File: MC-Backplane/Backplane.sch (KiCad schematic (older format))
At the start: 6 parts

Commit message: Add files via upload
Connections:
- net ADCSlots/24vP renamed 24V
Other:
- moved on the sheet: D?, F?, J?, R?, U?
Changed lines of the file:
@@
 $Descr A4 11693 8268
 encoding utf-8
-Sheet 1 5
+Sheet 1 6
 Title ""
 Date ""
@@
 $EndDescr
 $Sheet
-S 2000 5250 950  450
-U 61E8CAB3
-F0 "GateDriveSlots" 50
-F1 "GateDriveSlots.sch" 50
-F2 "24vP" I L 2000 5350 50
-$EndSheet
-$Sheet
-S 5000 5250 950  450
+S 4950 6200 950  450
 U 61E8CB73
 F0 "DeltaSigmaSlots" 50
 F1 "DeltaSigmasSlots.sch" 50
-F2 "24vP" I L 5000 5350 50
+F2 "24V" I L 4950 6300 50
 $EndSheet
 $Sheet
-S 8550 5250 950  450
+S 4950 4700 950  450
 U 61E8CB26
 F0 "ADCSlots" 50
 F1 "ADCSlots.sch" 50
-F2 "24vP" I L 8550 5350 50
+F2 "24V" I L 4950 4800 50
 $EndSheet
 $Comp
 L Device:D_Zener D?
 U 1 1 61EB8C1B
-P 5950 2500
-F 0 "D?" V 5904 2580 50  0000 L CNN
-F 1 "Zener BZX84C9V1-7-F" V 5995 2580 50  0000 L CNN
-F 2 "" H 5950 2500 50  0001 C CNN
-F 3 "https://www.digikey.com/en/products/detail/diodes-incorporated/BZX84C9V1-7-F/717755" H 5950 2500 50  0001 C CNN
-	1    5950 2500
+P 4050 2400
+F 0 "D?" V 4004 2480 50  0000 L CNN
+F 1 "Zener BZX84C9V1-7-F" V 4095 2480 50  0000 L CNN
+F 2 "" H 4050 2400 50  0001 C CNN
+F 3 "https://www.digikey.com/en/products/detail/diodes-incorporated/BZX84C9V1-7-F/717755" H 4050 2400 50  0001 C CNN
+	1    4050 2400
 	0    1    1    0
 $EndComp
@@
 L Device:R_Small_US R?
 U 1 1 61EBB5D2
-P 5100 3150
-F 0 "R?" H 5168 3196 50  0000 L CNN
-F 1 "3k" H 5168 3105 50  0000 L CNN
-F 2 "Resistor_SMD:R_1206_3216Metric" H 5100 3150 50  0001 C CNN
-F 3 "~" H 5100 3150 50  0001 C CNN
-	1    5100 3150
+P 3200 2850
+F 0 "R?" H 3268 2896 50  0000 L CNN
+F 1 "3k" H 3268 2805 50  0000 L CNN
+F 2 "Resistor_SMD:R_1206_3216Metric" H 3200 2850 50  0001 C CNN
+F 3 "~" H 3200 2850 50  0001 C CNN
+	1    3200 2850
 	1    0    0    -1
 $EndComp
 Wire Wire Line
-	5100 2500 5100 2750
+	3200 2500 3200 2650
 Wire Wire Line
-	5950 2650 5950 2750
+	4050 2550 4050 2650
 Wire Wire Line
-	5950 2750 5100 2750
-Connection ~ 5100 2750
+	4050 2650 3200 2650
+Connection ~ 3200 2650
 Wire Wire Line
-	5100 2750 5100 3050
+	3200 2650 3200 2750
 Wire Wire Line
-	5950 2350 5950 2200
+	4050 2250 4050 2200
 Wire Wire Line
-	5950 2200 5300 2200
-Connection ~ 5950 2200
+	4050 2200 3400 2200
 $Comp
 L power:GND #PWR0101
 U 1 1 61EBD36B
-P 5100 3600
-F 0 "#PWR0101" H 5100 3350 50  0001 C CNN
-F 1 "GND" H 5105 3427 50  0000 C CNN
-F 2 "" H 5100 3600 50  0001 C CNN
-F 3 "" H 5100 3600 50  0001 C CNN
-	1    5100 3600
+P 3200 3050
+F 0 "#PWR0101" H 3200 2800 50  0001 C CNN
+F 1 "GND" H 3205 2877 50  0000 C CNN
+F 2 "" H 3200 3050 50  0001 C CNN
+F 3 "" H 3200 3050 50  0001 C CNN
+	1    3200 3050
 	1    0    0    -1
 $EndComp
@@
 RDS of PMOS needs to be really small like miliohms.\n\nDrain current needs to be larger than what the load requires.\nVDS needs to be larger than the source voltage by a significant amount. 24V so around  45V-60V.\n\nThe Zener diode needs a voltage rating of just under VDS of the mosfet. \n\nnot sure about the resistors.
 Wire Wire Line
-	5100 3250 5100 3600
-Text Notes 4500 1800 0    50   ~ 0
+	3200 2950 3200 3050
+Text Notes 2600 1800 0    50   ~ 0
 Reverse Polarity Protection Circuit
 Text Notes 8500 900  0    50   ~ 0
 Global reset to/from all cards and DSP\nFO enable b/w DSP and FO card only
-Wire Wire Line
-	1200 4250 1200 5350
-Wire Wire Line
-	1200 5350 2000 5350
-Wire Wire Line
-	4750 5350 5000 5350
-Wire Wire Line
-	4750 4950 7250 4950
-Wire Wire Line
-	8150 4950 8150 5350
-Wire Wire Line
-	8150 5350 8550 5350
-Wire Wire Line
-	4750 4950 4750 5350
 $Comp
 L MC-Backplane:64600001223 U?
 U 1 1 61F13696
-P 3650 2400
-F 0 "U?" H 3650 2427 50  0000 C CNN
-F 1 "64600001223" H 3650 2336 50  0000 C CNN
-F 2 "" H 3650 2400 50  0001 C CNN
-F 3 "https://www.littelfuse.com/~/media/electronics/datasheets/fuse_blocks/littelfuse_fuse_block_646_datasheet.pdf.pdf" H 3650 2400 50  0001 C CNN
-	1    3650 2400
+P 2300 2400
+F 0 "U?" H 2300 2427 50  0000 C CNN
+F 1 "64600001223" H 2300 2336 50  0000 C CNN
+F 2 "" H 2300 2400 50  0001 C CNN
+F 3 "https://www.littelfuse.com/~/media/electronics/datasheets/fuse_blocks/littelfuse_fuse_block_646_datasheet.pdf.pdf" H 2300 2400 50  0001 C CNN
+	1    2300 2400
 	1    0    0    -1
 $EndComp
 Wire Wire Line
-	4050 2200 4900 2200
-Wire Wire Line
-	5950 2200 7250 2200
-Wire Wire Line
-	1200 4250 7250 4250
-Wire Wire Line
-	7250 4250 7250 2200
-Connection ~ 7250 2200
-Wire Wire Line
-	7250 2200 10000 2200
-Wire Wire Line
-	7250 4250 7250 4950
-Connection ~ 7250 4250
-Connection ~ 7250 4950
-Wire Wire Line
-	7250 4950 8150 4950
+	2700 2200 3000 2200
 $Comp
 L Connector:Barrel_Jack J?
 U 1 1 61F21CB0
-P 1850 2300
-F 0 "J?" H 1907 2625 50  0000 C CNN
-F 1 "Barrel_Jack" H 1907 2534 50  0000 C CNN
-F 2 "" H 1900 2260 50  0001 C CNN
-F 3 "~" H 1900 2260 50  0001 C CNN
-	1    1850 2300
+P 1300 2300
+F 0 "J?" H 1357 2625 50  0000 C CNN
+F 1 "Barrel_Jack" H 1357 2534 50  0000 C CNN
+F 2 "" H 1350 2260 50  0001 C CNN
+F 3 "~" H 1350 2260 50  0001 C CNN
+	1    1300 2300
 	1    0    0    -1
 $EndComp
 Wire Wire Line
-	2150 2200 3250 2200
+	1600 2200 1900 2200
 $Comp
 L Device:Fuse F?
 U 1 1 61F2B17A
-P 3650 1700
-F 0 "F?" V 3453 1700 50  0000 C CNN
-F 1 "Fuse" V 3544 1700 50  0000 C CNN
-F 2 "" V 3580 1700 50  0001 C CNN
-F 3 "~" H 3650 1700 50  0001 C CNN
-	1    3650 1700
+P 2300 1700
+F 0 "F?" V 2103 1700 50  0000 C CNN
+F 1 "Fuse" V 2194 1700 50  0000 C CNN
+F 2 "" V 2230 1700 50  0001 C CNN
+F 3 "~" H 2300 1700 50  0001 C CNN
+	1    2300 1700
 	0    1    1    0
 $EndComp
 Wire Wire Line
-	3500 1700 3500 1950
+	2150 1700 2150 1950
 Wire Wire Line
-	3800 1950 3800 1700
-Text Notes 1400 2650 0    50   ~ 0
+	2450 1950 2450 1700
+Text Notes 850  2650 0    50   ~ 0
 maybe:  5.5mm barrel jack? \nwith 2.1mm center pole
 $Comp
 L MC-Backplane:SISS05DN-T1-GE3 U?
 U 1 1 61F2E911
-P 5600 2200
-F 0 "U?" V 5842 2700 50  0000 C CNN
-F 1 "SISS05DN-T1-GE3" V 5751 2700 50  0000 C CNN
-F 2 "" H 5600 2200 50  0001 C CNN
-F 3 "" H 5600 2200 50  0001 C CNN
-	1    5600 2200
+P 3700 2200
+F 0 "U?" V 3942 2700 50  0000 C CNN
+F 1 "SISS05DN-T1-GE3" V 3851 2700 50  0000 C CNN
+F 2 "" H 3700 2200 50  0001 C CNN
+F 3 "" H 3700 2200 50  0001 C CNN
+	1    3700 2200
 	0    -1   -1   0
 $EndComp
 $Sheet
-S 10000 2100 950  1900
+S 9400 1700 1000 3950
 U 61E8CBE3
 F0 "DSPSlot" 50
 F1 "DSPSlot.sch" 50
-F2 "24vP" I L 10000 2200 50
+F2 "24V" I L 9400 1800 50
 $EndSheet
+$Sheet
+S 1750 3550 1150 1450
+U 61E8CAB3
+F0 "GateDriveSlots" 50
+F1 "GateDriveSlots.sch" 50
+F2 "24V" I L 1750 3600 50
+F3 "GND" I R 2900 4950 50
+F4 "EPWM1_1A" I L 1750 3750 50
+F5 "EPWM1_1B" I L 1750 3850 50
+F6 "RESET1_1" I L 1750 3950 50
+F7 "STATUS1_1" O R 2900 3600 50
+F8 "EPWM1_2A" I L 1750 4050 50
+F9 "EPWM1_2B" I L 1750 4150 50
+F10 "RESET1_2" I L 1750 4250 50
+F11 "STATUS1_2" O R 2900 3700 50
+F12 "EPWM3_1A" I L 1750 4400 50
+F13 "EPWM3_1B" I L 1750 4500 50
+F14 "STATUS3_1" O R 2900 4000 50
+F15 "EPWM3_2A" I L 1750 4650 50
+F16 "EPWM3_2B" I L 1750 4750 50
+F17 "RESET3_2" I L 1750 4850 50
+F18 "EPWM2_1A" I R 2900 4300 50
+F19 "EPWM2_1B" I R 2900 4400 50
+F20 "RESET2_1" I R 2900 4500 50
+F21 "STATUS2_1" O R 2900 3800 50
+F22 "EPWM2_2A" I R 2900 4600 50
+F23 "EPWM2_2B" I R 2900 4700 50
+F24 "RESET2_2" I R 2900 4800 50
+F25 "STATUS2_2" O R 2900 3900 50
+F26 "STATUS3_2" O R 2900 4100 50
+$EndSheet
+$Sheet
+S 1750 5600 1150 1500
+U 61F59C33
+F0 "GateDriveSlots4-6" 50
+F1 "GateDriveSlots4-6.sch" 50
+F2 "24V" I L 1750 5700 50
+$EndSheet
+Wire Wire Line
+	4050 2200 4700 2200
+Connection ~ 4050 2200
+Text GLabel 4700 2200 2    50   Output ~ 0
+24V
+Text GLabel 1750 3600 0    50   Input ~ 0
+24V
+Text GLabel 1750 5700 0    50   Input ~ 0
+24V
+Text GLabel 4950 6300 0    50   Input ~ 0
+24V
+Text GLabel 4950 4800 0    50   Input ~ 0
+24V
+Text GLabel 9400 1800 0    50   Input ~ 0
+24V
 $EndSCHEMATC

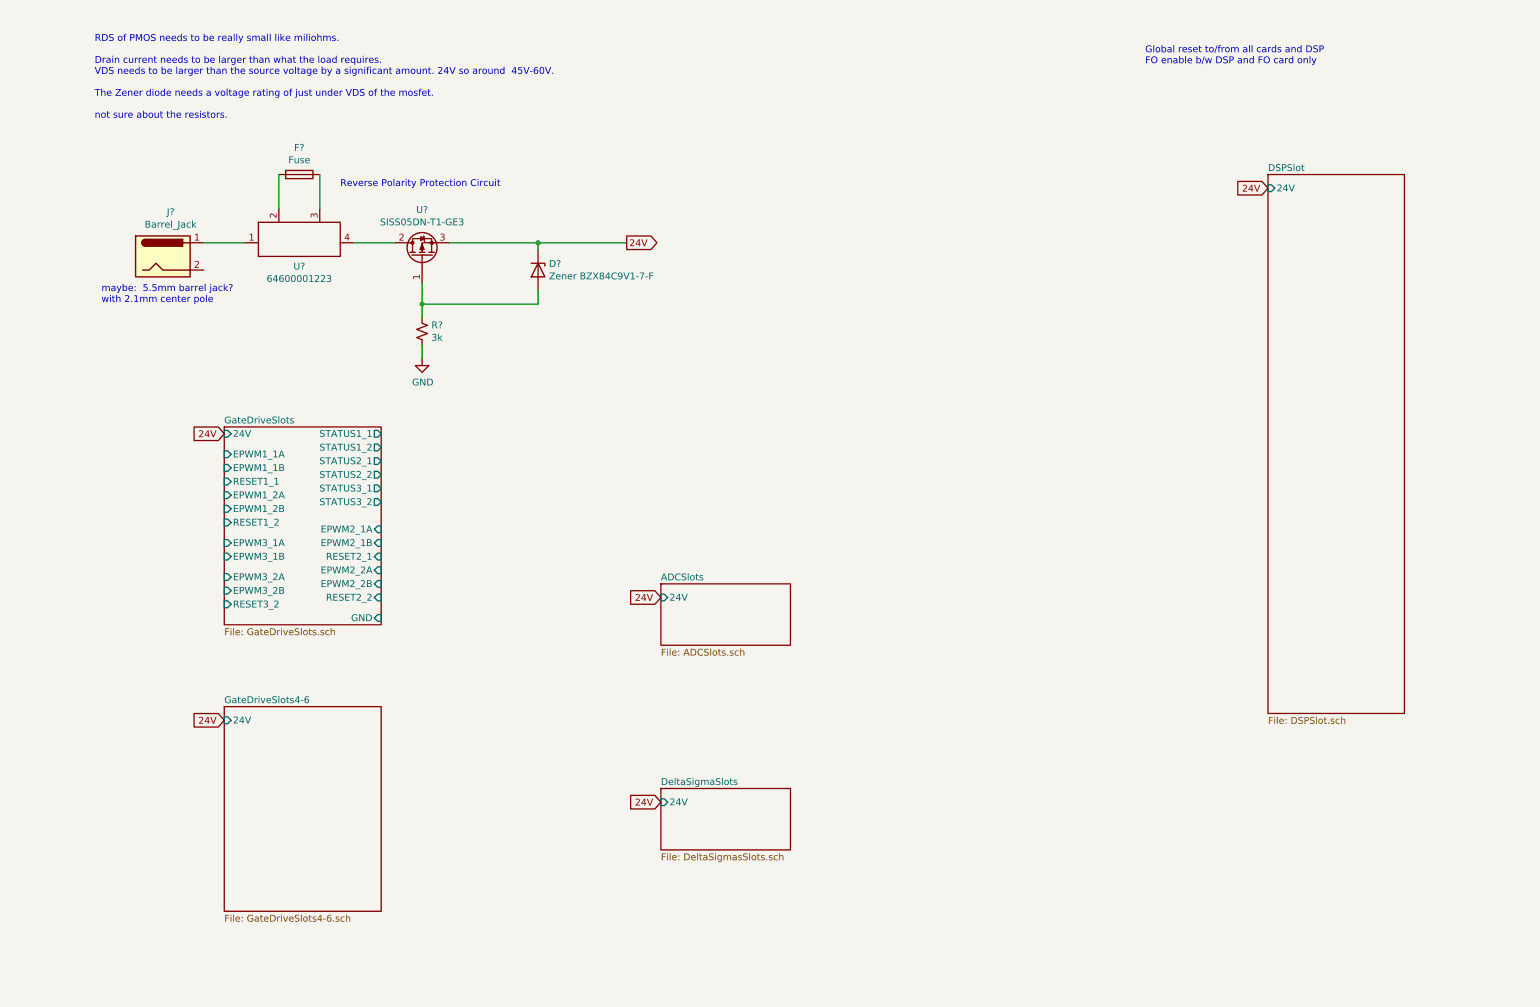
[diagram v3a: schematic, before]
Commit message: added signals for FO slots
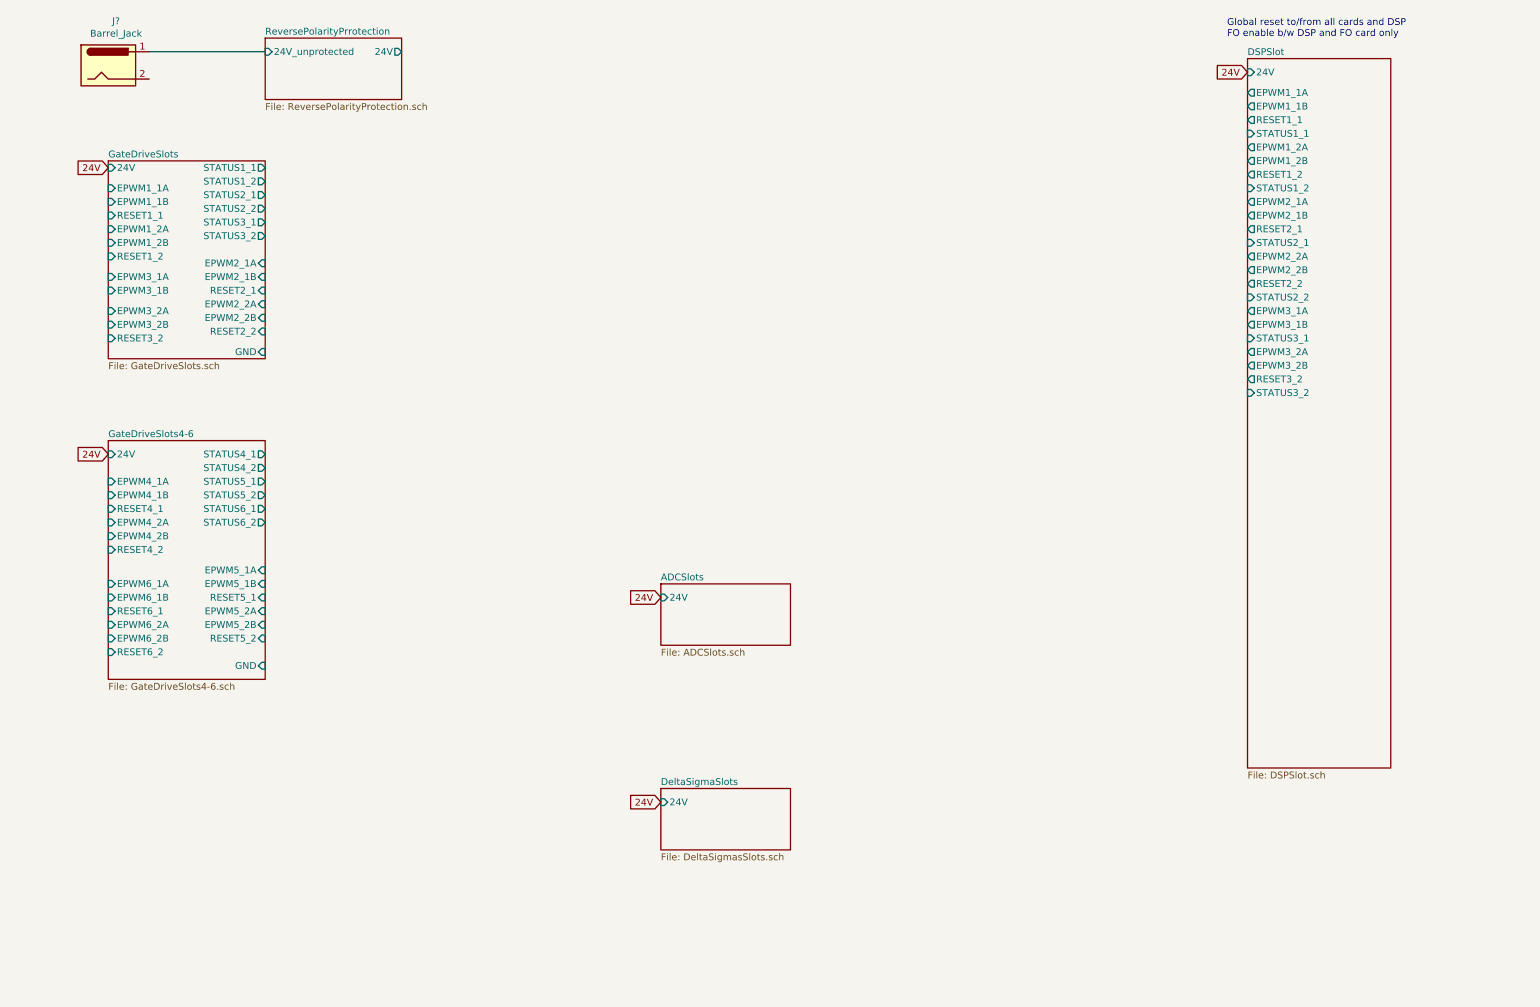
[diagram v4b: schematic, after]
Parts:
- removed D?: Zener BZX84C9V1-7-F, symbol Device:D_Zener
- removed F?: Fuse, symbol Device:Fuse
- removed R?: 3k, Resistor_SMD:R_1206_3216Metric, symbol Device:R_Small_US
- removed U?: 64600001223, symbol MC-Backplane:64600001223
- removed U?: SISS05DN-T1-GE3, symbol MC-Backplane:SISS05DN-T1-GE3
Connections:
- net ReversePolarityPrrotection/24V_unprotected: now reaches J?.1
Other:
- note removed: "RDS of PMOS needs to be really small like miliohms.\n\nDrain current needs to be larger than what the load requires.\nVDS needs to be larger than the source voltage by a significant amount. 24V so around 45V-60V.\n\nThe Zener diode needs a voltage rating of just under VDS of the mosfet. \n\nnot sure about the resistors."
- note removed: "Reverse Polarity Protection Circuit"
- note removed: "maybe: 5.5mm barrel jack? \nwith 2.1mm center pole"
- moved on the sheet: J?
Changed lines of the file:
@@
 $Descr A4 11693 8268
 encoding utf-8
-Sheet 1 6
+Sheet 1 7
 Title ""
 Date ""
@@
 F2 "24V" I L 4950 4800 50
 $EndSheet
-$Comp
-L Device:D_Zener D?
-U 1 1 61EB8C1B
-P 4050 2400
-F 0 "D?" V 4004 2480 50  0000 L CNN
-F 1 "Zener BZX84C9V1-7-F" V 4095 2480 50  0000 L CNN
-F 2 "" H 4050 2400 50  0001 C CNN
-F 3 "https://www.digikey.com/en/products/detail/diodes-incorporated/BZX84C9V1-7-F/717755" H 4050 2400 50  0001 C CNN
-	1    4050 2400
-	0    1    1    0
-$EndComp
-$Comp
-L Device:R_Small_US R?
-U 1 1 61EBB5D2
-P 3200 2850
-F 0 "R?" H 3268 2896 50  0000 L CNN
-F 1 "3k" H 3268 2805 50  0000 L CNN
-F 2 "Resistor_SMD:R_1206_3216Metric" H 3200 2850 50  0001 C CNN
-F 3 "~" H 3200 2850 50  0001 C CNN
-	1    3200 2850
-	1    0    0    -1
-$EndComp
-Wire Wire Line
-	3200 2500 3200 2650
-Wire Wire Line
-	4050 2550 4050 2650
-Wire Wire Line
-	4050 2650 3200 2650
-Connection ~ 3200 2650
-Wire Wire Line
-	3200 2650 3200 2750
-Wire Wire Line
-	4050 2250 4050 2200
-Wire Wire Line
-	4050 2200 3400 2200
-$Comp
-L power:GND #PWR0101
-U 1 1 61EBD36B
-P 3200 3050
-F 0 "#PWR0101" H 3200 2800 50  0001 C CNN
-F 1 "GND" H 3205 2877 50  0000 C CNN
-F 2 "" H 3200 3050 50  0001 C CNN
-F 3 "" H 3200 3050 50  0001 C CNN
-	1    3200 3050
-	1    0    0    -1
-$EndComp
-Text Notes 800  1300 0    50   ~ 0
-RDS of PMOS needs to be really small like miliohms.\n\nDrain current needs to be larger than what the load requires.\nVDS needs to be larger than the source voltage by a significant amount. 24V so around  45V-60V.\n\nThe Zener diode needs a voltage rating of just under VDS of the mosfet. \n\nnot sure about the resistors.
-Wire Wire Line
-	3200 2950 3200 3050
-Text Notes 2600 1800 0    50   ~ 0
-Reverse Polarity Protection Circuit
-Text Notes 8500 900  0    50   ~ 0
+Text Notes 9100 700  0    50   ~ 0
 Global reset to/from all cards and DSP\nFO enable b/w DSP and FO card only
-$Comp
-L MC-Backplane:64600001223 U?
-U 1 1 61F13696
-P 2300 2400
-F 0 "U?" H 2300 2427 50  0000 C CNN
-F 1 "64600001223" H 2300 2336 50  0000 C CNN
-F 2 "" H 2300 2400 50  0001 C CNN
-F 3 "https://www.littelfuse.com/~/media/electronics/datasheets/fuse_blocks/littelfuse_fuse_block_646_datasheet.pdf.pdf" H 2300 2400 50  0001 C CNN
-	1    2300 2400
-	1    0    0    -1
-$EndComp
-Wire Wire Line
-	2700 2200 3000 2200
 $Comp
 L Connector:Barrel_Jack J?
 U 1 1 61F21CB0
-P 1300 2300
-F 0 "J?" H 1357 2625 50  0000 C CNN
-F 1 "Barrel_Jack" H 1357 2534 50  0000 C CNN
-F 2 "" H 1350 2260 50  0001 C CNN
-F 3 "~" H 1350 2260 50  0001 C CNN
-	1    1300 2300
+P 900 900
+F 0 "J?" H 957 1225 50  0000 C CNN
+F 1 "Barrel_Jack" H 957 1134 50  0000 C CNN
+F 2 "" H 950 860 50  0001 C CNN
+F 3 "~" H 950 860 50  0001 C CNN
+	1    900  900
 	1    0    0    -1
 $EndComp
-Wire Wire Line
-	1600 2200 1900 2200
-$Comp
-L Device:Fuse F?
-U 1 1 61F2B17A
-P 2300 1700
-F 0 "F?" V 2103 1700 50  0000 C CNN
-F 1 "Fuse" V 2194 1700 50  0000 C CNN
-F 2 "" V 2230 1700 50  0001 C CNN
-F 3 "~" H 2300 1700 50  0001 C CNN
-	1    2300 1700
-	0    1    1    0
-$EndComp
-Wire Wire Line
-	2150 1700 2150 1950
-Wire Wire Line
-	2450 1950 2450 1700
-Text Notes 850  2650 0    50   ~ 0
-maybe:  5.5mm barrel jack? \nwith 2.1mm center pole
-$Comp
-L MC-Backplane:SISS05DN-T1-GE3 U?
-U 1 1 61F2E911
-P 3700 2200
-F 0 "U?" V 3942 2700 50  0000 C CNN
-F 1 "SISS05DN-T1-GE3" V 3851 2700 50  0000 C CNN
-F 2 "" H 3700 2200 50  0001 C CNN
-F 3 "" H 3700 2200 50  0001 C CNN
-	1    3700 2200
-	0    -1   -1   0
-$EndComp
 $Sheet
-S 9400 1700 1000 3950
+S 9250 850  1050 5200
 U 61E8CBE3
 F0 "DSPSlot" 50
 F1 "DSPSlot.sch" 50
-F2 "24V" I L 9400 1800 50
+F2 "24V" I L 9250 950 50
+F3 "EPWM1_1A" O L 9250 1100 50
+F4 "EPWM1_1B" O L 9250 1200 50
+F5 "RESET1_1" O L 9250 1300 50
+F6 "STATUS1_1" I L 9250 1400 50
+F7 "EPWM1_2A" O L 9250 1500 50
+F8 "EPWM1_2B" O L 9250 1600 50
+F9 "RESET1_2" O L 9250 1700 50
+F10 "STATUS1_2" I L 9250 1800 50
+F11 "EPWM2_1A" O L 9250 1900 50
+F12 "EPWM2_1B" O L 9250 2000 50
+F13 "RESET2_1" O L 9250 2100 50
+F14 "STATUS2_1" I L 9250 2200 50
+F15 "EPWM2_2A" O L 9250 2300 50
+F16 "EPWM2_2B" O L 9250 2400 50
+F17 "RESET2_2" O L 9250 2500 50
+F18 "STATUS2_2" I L 9250 2600 50
+F19 "EPWM3_1A" O L 9250 2700 50
+F20 "EPWM3_1B" O L 9250 2800 50
+F21 "STATUS3_1" I L 9250 2900 50
+F22 "EPWM3_2A" O L 9250 3000 50
+F23 "EPWM3_2B" O L 9250 3100 50
+F24 "RESET3_2" O L 9250 3200 50
+F25 "STATUS3_2" I L 9250 3300 50
 $EndSheet
 $Sheet
-S 1750 3550 1150 1450
+S 900  1600 1150 1450
 U 61E8CAB3
 F0 "GateDriveSlots" 50
 F1 "GateDriveSlots.sch" 50
-F2 "24V" I L 1750 3600 50
-F3 "GND" I R 2900 4950 50
-F4 "EPWM1_1A" I L 1750 3750 50
-F5 "EPWM1_1B" I L 1750 3850 50
-F6 "RESET1_1" I L 1750 3950 50
-F7 "STATUS1_1" O R 2900 3600 50
-F8 "EPWM1_2A" I L 1750 4050 50
-F9 "EPWM1_2B" I L 1750 4150 50
-F10 "RESET1_2" I L 1750 4250 50
-F11 "STATUS1_2" O R 2900 3700 50
-F12 "EPWM3_1A" I L 1750 4400 50
-F13 "EPWM3_1B" I L 1750 4500 50
-F14 "STATUS3_1" O R 2900 4000 50
-F15 "EPWM3_2A" I L 1750 4650 50
-F16 "EPWM3_2B" I L 1750 4750 50
-F17 "RESET3_2" I L 1750 4850 50
-F18 "EPWM2_1A" I R 2900 4300 50
-F19 "EPWM2_1B" I R 2900 4400 50
-F20 "RESET2_1" I R 2900 4500 50
-F21 "STATUS2_1" O R 2900 3800 50
-F22 "EPWM2_2A" I R 2900 4600 50
-F23 "EPWM2_2B" I R 2900 4700 50
-F24 "RESET2_2" I R 2900 4800 50
-F25 "STATUS2_2" O R 2900 3900 50
-F26 "STATUS3_2" O R 2900 4100 50
+F2 "24V" I L 900 1650 50
+F3 "GND" I R 2050 3000 50
+F4 "EPWM1_1A" I L 900 1800 50
+F5 "EPWM1_1B" I L 900 1900 50
+F6 "RESET1_1" I L 900 2000 50
+F7 "STATUS1_1" O R 2050 1650 50
+F8 "EPWM1_2A" I L 900 2100 50
+F9 "EPWM1_2B" I L 900 2200 50
+F10 "RESET1_2" I L 900 2300 50
+F11 "STATUS1_2" O R 2050 1750 50
+F12 "EPWM3_1A" I L 900 2450 50
+F13 "EPWM3_1B" I L 900 2550 50
+F14 "STATUS3_1" O R 2050 2050 50
+F15 "EPWM3_2A" I L 900 2700 50
+F16 "EPWM3_2B" I L 900 2800 50
+F17 "RESET3_2" I L 900 2900 50
+F18 "EPWM2_1A" I R 2050 2350 50
+F19 "EPWM2_1B" I R 2050 2450 50
+F20 "RESET2_1" I R 2050 2550 50
+F21 "STATUS2_1" O R 2050 1850 50
+F22 "EPWM2_2A" I R 2050 2650 50
+F23 "EPWM2_2B" I R 2050 2750 50
+F24 "RESET2_2" I R 2050 2850 50
+F25 "STATUS2_2" O R 2050 1950 50
+F26 "STATUS3_2" O R 2050 2150 50
 $EndSheet
-$Sheet
-S 1750 5600 1150 1500
-U 61F59C33
-F0 "GateDriveSlots4-6" 50
-F1 "GateDriveSlots4-6.sch" 50
-F2 "24V" I L 1750 5700 50
-$EndSheet
-Wire Wire Line
-	4050 2200 4700 2200
-Connection ~ 4050 2200
-Text GLabel 4700 2200 2    50   Output ~ 0
-24V
-Text GLabel 1750 3600 0    50   Input ~ 0
-24V
-Text GLabel 1750 5700 0    50   Input ~ 0
+Text GLabel 900  1650 0    50   Input ~ 0
 24V
 Text GLabel 4950 6300 0    50   Input ~ 0
@@
 Text GLabel 4950 4800 0    50   Input ~ 0
 24V
-Text GLabel 9400 1800 0    50   Input ~ 0
+Text GLabel 9250 950  0    50   Input ~ 0
+24V
+$Sheet
+S 900  3650 1150 1750
+U 61F59C33
+F0 "GateDriveSlots4-6" 50
+F1 "GateDriveSlots4-6.sch" 50
+F2 "24V" I L 900 3750 50
+F3 "GND" I R 2050 5300 50
+F4 "EPWM4_1A" I L 900 3950 50
+F5 "EPWM4_1B" I L 900 4050 50
+F6 "RESET4_1" I L 900 4150 50
+F7 "STATUS4_1" O R 2050 3750 50
+F8 "EPWM4_2A" I L 900 4250 50
+F9 "EPWM4_2B" I L 900 4350 50
+F10 "RESET4_2" I L 900 4450 50
+F11 "STATUS4_2" O R 2050 3850 50
+F12 "STATUS6_2" O R 2050 4250 50
+F13 "RESET6_2" I L 900 5200 50
+F14 "EPWM6_2B" I L 900 5100 50
+F15 "EPWM6_2A" I L 900 5000 50
+F16 "STATUS6_1" O R 2050 4150 50
+F17 "RESET6_1" I L 900 4900 50
+F18 "EPWM6_1B" I L 900 4800 50
+F19 "EPWM6_1A" I L 900 4700 50
+F20 "STATUS5_2" O R 2050 4050 50
+F21 "RESET5_2" I R 2050 5100 50
+F22 "EPWM5_2B" I R 2050 5000 50
+F23 "EPWM5_2A" I R 2050 4900 50
+F24 "STATUS5_1" O R 2050 3950 50
+F25 "RESET5_1" I R 2050 4800 50
+F26 "EPWM5_1B" I R 2050 4700 50
+F27 "EPWM5_1A" I R 2050 4600 50
+$EndSheet
+$Sheet
+S 2050 700  1000 450
+U 61FBA43E
+F0 "ReversePolarityPrrotection" 50
+F1 "ReversePolarityProtection.sch" 50
+F2 "24V" O R 3050 800 50
+F3 "24V_unprotected" I L 2050 800 50
+$EndSheet
+Wire Wire Line
+	1200 800  2050 800
+Text GLabel 900  3750 0    50   Input ~ 0
 24V
 $EndSCHEMATC
